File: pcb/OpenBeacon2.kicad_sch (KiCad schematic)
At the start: 74 parts, among them J1 Bias V, J10 UART, J11 BNC, J16 SMA CLKIN, J2 PAI+, J3 PAI-, J4 Digital IO, J5 ADC Inputs, J6 SMA, J8 I2C Bus, J9 GND, Q1 2N7002, Q2 MMBT4403, Q3 2SK3074, Q4 2N7002, Q5 2N7002, U1 TLV61046A, U2 ASTX-H11-25.000MHZ-T, U3 SN74LVC1G17, U4 SI5351C-B-GMR, U5 MCP4725A1T-E/CH, U6 128x32 OLED, U8 24AA64T

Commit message: BT1: KH-BS1220-2-SMT footprint from LCSC C5365932; J6/J16: Si5351BCBreakout SMA-ENDLAUNCH footprint, BWSMA-KE-P001 C496550; project-local OB2 footprint lib
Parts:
- J16: footprint EtherkitKicadLibrary:SMA-ENDLAUNCH -> OB2:SMA-ENDLAUNCH
- J6: footprint EtherkitKicadLibrary:SMA-ENDLAUNCH -> OB2:SMA-ENDLAUNCH; LCSC (none) -> C496550; MPN (none) -> BWSMA-KE-P001; Manufacturer (none) -> BAT Wireless
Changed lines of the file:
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@@
 			)
 		)
-		(property "Footprint" "EtherkitKicadLibrary:SMA-ENDLAUNCH"
-			(at 172.72 185.42 0)
-			(effects
-				(font
-					(size 1.27 1.27)
-				)
-				(hide yes)
-			)
-		)
-		(property "Datasheet" ""
+		(property "Footprint" "OB2:SMA-ENDLAUNCH"
+			(at 172.72 185.42 0)
+			(effects
+				(font
+					(size 1.27 1.27)
+				)
+				(hide yes)
+			)
+		)
+		(property "Datasheet" ""
+			(at 172.72 185.42 0)
+			(effects
+				(font
+					(size 1.27 1.27)
+				)
+				(hide yes)
+			)
+		)
+		(property "LCSC" "C496550"
+			(at 172.72 185.42 0)
+			(effects
+				(font
+					(size 1.27 1.27)
+				)
+				(hide yes)
+			)
+		)
+		(property "Manufacturer" "BAT Wireless"
+			(at 172.72 185.42 0)
+			(effects
+				(font
+					(size 1.27 1.27)
+				)
+				(hide yes)
+			)
+		)
+		(property "MPN" "BWSMA-KE-P001"
 			(at 172.72 185.42 0)
 			(effects
@@
 			)
 		)
-		(property "Footprint" "EtherkitKicadLibrary:SMA-ENDLAUNCH"
+		(property "Footprint" "OB2:SMA-ENDLAUNCH"
 			(at 33.02 220.98 0)
 			(effects

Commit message: Restore hand-wired root sheet, add Si5351C wired, split root across two A4 sheets
Root (A4) is the c2d4355 drawing with continuous wires: boost, keying, PA,
bias DAC, filter bank, BNC out, plus the Si5351C (U4, C14/C50-C53, J6 CLK2,
J16 CLKIN with R43/C54/R44/R45, R46 INTR pull-up, R47 CAL_CLK) drawn wired.
I/O headers, OLED/buttons, I2C level shift and EEPROM move unchanged to the
new io_ui.kicad_sch (A4). Netlist node sets identical to c569d37.
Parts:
- removed C1, C10, C11, C14, C17, C18, C19, C20, C21, C22, C23, C24, C5, C6, C8: 100n, Capacitor_SMD:C_0805_2012Metric, symbol Device:C_Small
- removed C2: 4.7u, Capacitor_SMD:C_0805_2012Metric, symbol Device:C_Small
- removed C3: 10u, Capacitor_SMD:C_0805_2012Metric, symbol Device:C_Small
- removed C4: 10n, Capacitor_SMD:C_0805_2012Metric, symbol Device:C_Small
- removed C50, C51, C52, C53, C54: 100n, Capacitor_SMD:C_0603_1608Metric, symbol Device:C_Small
- removed C7, C9: 1u, Capacitor_SMD:C_0805_2012Metric, symbol Device:C_Small
- removed J10: UART, Connector_PinHeader_2.54mm:PinHeader_1x04_P2.54mm_Vertical, symbol Connector_Generic:Conn_01x04
- removed J4: Digital IO, Connector_PinHeader_2.54mm:PinHeader_1x04_P2.54mm_Vertical, symbol Connector_Generic:Conn_01x04
- removed J5: ADC Inputs, Connector_PinHeader_2.54mm:PinHeader_1x06_P2.54mm_Vertical, symbol Connector_Generic:Conn_01x06
- removed J8: I2C Bus, Connector_PinHeader_2.54mm:PinHeader_1x04_P2.54mm_Vertical, symbol Connector_Generic:Conn_01x04
- removed Q4, Q5: 2N7002, EtherkitKicadLibrary:SOT23-2N7002, symbol EtherkitKicadLibrary:MOS_N
- removed R1, R2, R3: 22k, Resistor_SMD:R_0805_2012Metric, symbol Device:R_Small_US
- removed R11, R12, R14, R15, R5: 3.3k, Resistor_SMD:R_0805_2012Metric, symbol Device:R_Small_US
- removed R43: 49.9, Resistor_SMD:R_0603_1608Metric, symbol Device:R_Small_US
- removed R44, R45, R46: 10k, Resistor_SMD:R_0603_1608Metric, symbol Device:R_Small_US
- removed R47: 33, Resistor_SMD:R_0603_1608Metric, symbol Device:R_Small_US
- removed R6: 10, Resistor_SMD:R_0805_2012Metric, symbol Device:R_Small_US
- removed R7: 56, Resistor_SMD:R_0805_2012Metric, symbol Device:R_Small_US
- removed R8: 1 1%, Resistor_SMD:R_0805_2012Metric, symbol Device:R_Small_US
- removed S1: Menu 1, EtherkitKicadLibrary:Omron_B3F-1052, symbol EtherkitKicadLibrary:PUSHBUTTON_TACTILE
- removed S2: Menu 2, EtherkitKicadLibrary:Omron_B3F-1052, symbol EtherkitKicadLibrary:PUSHBUTTON_TACTILE
- removed S3: Left, EtherkitKicadLibrary:Omron_B3F-1052, symbol EtherkitKicadLibrary:PUSHBUTTON_TACTILE
- removed S4: Down, EtherkitKicadLibrary:Omron_B3F-1052, symbol EtherkitKicadLibrary:PUSHBUTTON_TACTILE
- removed S5: Up, EtherkitKicadLibrary:Omron_B3F-1052, symbol EtherkitKicadLibrary:PUSHBUTTON_TACTILE
- removed S6: Back, EtherkitKicadLibrary:Omron_B3F-1052, symbol EtherkitKicadLibrary:PUSHBUTTON_TACTILE
- removed S7: Right, EtherkitKicadLibrary:Omron_B3F-1052, symbol EtherkitKicadLibrary:PUSHBUTTON_TACTILE
- removed U6: 128x32 OLED, EtherkitKicadLibrary:128x32OLED, symbol EtherkitKicadLibrary:128x32OLED
- removed U8: 24AA64T, Package_TO_SOT_SMD:SOT-23-5, symbol EtherkitKicadLibrary:24AA64T
- added C1, C10, C11, C14, C5, C6, C8: 100n, Capacitor_SMD:C_0805_2012Metric, symbol EtherkitKicadLibrary:C
- added C2: 4.7u, Capacitor_SMD:C_0805_2012Metric, symbol EtherkitKicadLibrary:C
- added C3: 10u, Capacitor_SMD:C_0805_2012Metric, symbol EtherkitKicadLibrary:C
- added C4: 10n, Capacitor_SMD:C_0805_2012Metric, symbol EtherkitKicadLibrary:C
- added C50, C51, C52, C53, C54: 100n, Capacitor_SMD:C_0603_1608Metric, symbol EtherkitKicadLibrary:C
- added C7, C9: 1u, Capacitor_SMD:C_0805_2012Metric, symbol EtherkitKicadLibrary:C
- added R1, R2, R3: 22k, Resistor_SMD:R_0805_2012Metric, symbol EtherkitKicadLibrary:R
- added R43: 49.9, Resistor_SMD:R_0603_1608Metric, symbol EtherkitKicadLibrary:R
- added R44, R45, R46: 10k, Resistor_SMD:R_0603_1608Metric, symbol EtherkitKicadLibrary:R
- added R47: 33, Resistor_SMD:R_0603_1608Metric, symbol EtherkitKicadLibrary:R
- added R5: 3.3k, Resistor_SMD:R_0805_2012Metric, symbol EtherkitKicadLibrary:R
- added R6: 10, Resistor_SMD:R_0805_2012Metric, symbol EtherkitKicadLibrary:R
- added R7: 56, Resistor_SMD:R_0805_2012Metric, symbol EtherkitKicadLibrary:R
- added R8: 1 1%, Resistor_SMD:R_0805_2012Metric, symbol EtherkitKicadLibrary:R
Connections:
- net +3.3V: now also C14.1, C50.1, C51.1, C52.1, C53.1, C6.1, R44.1, R46.1
- net +5V: now also C1.1, C10.1, C2.1
- net CAL_CLK: now also R47.2
- net GND: now also C1.2, C10.2, C14.2, C2.2, C3.2, C50.2, C51.2, C52.2, C53.2, C6.2, C7.2, C9.2, R1.2, R43.2, R45.2
- net SI_INTR: now also R46.2
- net TX: now also R1.1
- net at J16.1 (In): now also C54.1, R43.1
- net at U4.19 (CLK4): now also R47.1
- net BOOST_SW: no longer names the net of L1.1, U1.1 (SW)
- net CLK2_SMA: no longer names the net of J6.1 (In), U4.9 (CLK2)
- net LPF_OUT renamed Filter Bank/LPF_OUT
- net PAI_N: no longer names the net of J3.1 (P1), L2.1
- net PAI_N: now also R8.1
- net PAI_P: no longer names the net of J2.1 (P1)
- net PAI_P: now also C7.1, R6.1, R8.2
- net PA_BIAS: no longer names the net of J1.1 (P1), U5.1 (VOUT)
- net PA_BIAS: now also C9.1, R7.2
- net PA_DRAIN: no longer names the net of L2.2, Q3.3 (D)
- net PA_DRAIN: now also C11.2, C8.1
- net PA_DRIVE: no longer names the net of U3.4
- net PA_DRIVE: now also C5.2, R5.2
- net PA_GATE: no longer names the net of Q3.2 (G)
- net PA_GATE: now also C5.1, R7.1
- net PA_SW_B: no longer names the net of Q2.2 (B)
- net PA_SW_B: now also C4.2, R2.2, R3.1
- net PA_VDD: no longer names the net of Q2.3 (C)
- net PA_VDD: now also C4.1, R6.2
- net SI_CLKIN: no longer names the net of U4.6 (CLKIN)
- net SI_CLKIN: now also C54.2, R44.2, R45.1
- net SI_XA: no longer names the net of R4.2, U4.1 (XA)
- net TCXO_OUT: no longer names the net of R4.1, U2.3 (OUT)
- net TX_N: no longer names the net of Q1.3 (D)
- net TX_N: now also R3.2
- net VBOOST: no longer names the net of Q2.1 (E), U1.5 (VO)
- net VBOOST: now also C3.1, R2.1
- new net: C8.2, R5.1
- new net Filter Bank/LPF_IN: C11.1
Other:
- added sheet I/O + UI (io_ui.kicad_sch)
- note added: "Boost Converter"
- note added: "Keying"
- note added: "Low-Pass Filter Bank (sheet 3)"
- note added: "PA Bias"
- note added: "Power Amplifier"
- note added: "Si5351C PLL"
- note removed: "12 V boost (TLV61046A)"
- note removed: "I/O headers"
- note removed: "I2C 3.3 V <-> 5 V level shift (OLED, DAC) + 24AA64 EEPROM"
- note removed: "J16 CLKIN (Si5351-B DS rev 1.3 Table 6, Table 16): 10-100 MHz, VIL < 0.3 VDD, VIH > 0.7 VDD, max 3.6 V; input not pulled internally. R43 terminates 50 ohm; C54 AC-couples; R44/R45 bias CLKIN at VDD/2. Sine needs >= 1.32 Vpp (+6.4 dBm) and <= 3.9 Vpp (+15.8 dBm). XB open (TCXO on XA, DS 6.6). OEB tied low = outputs enabled. INTR open drain, R46 10k (> 4.7k, DS Table 16) -> SI_INTR (PB3). CLK0 -> U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"
- note removed: "PAI+/PAI- = PA current-sense test points across R8 (1 ohm)."
- note removed: "Power amplifier (2SK3074) + bias DAC (MCP4725)"
- note removed: "Sub-sheets: Filter Bank (LPF_IN/LPF_OUT, BAND_A/B), MCU + USB (AVR128DA48, CP2102N, 3.3 V), GPS (MAX-M10S). They connect through the global labels."
- note removed: "Synth: Si5351C + 25 MHz TCXO on XA + external reference on CLKIN (J16)"
- note removed: "TX keying + PA supply switch"
- note removed: "U1 FB tied to VIN = fixed 12 V output (TLV61046A DS). C2 input, C3 output, both beside U1."
- note removed: "User interface: OLED + buttons (100n debounce beside each button)"

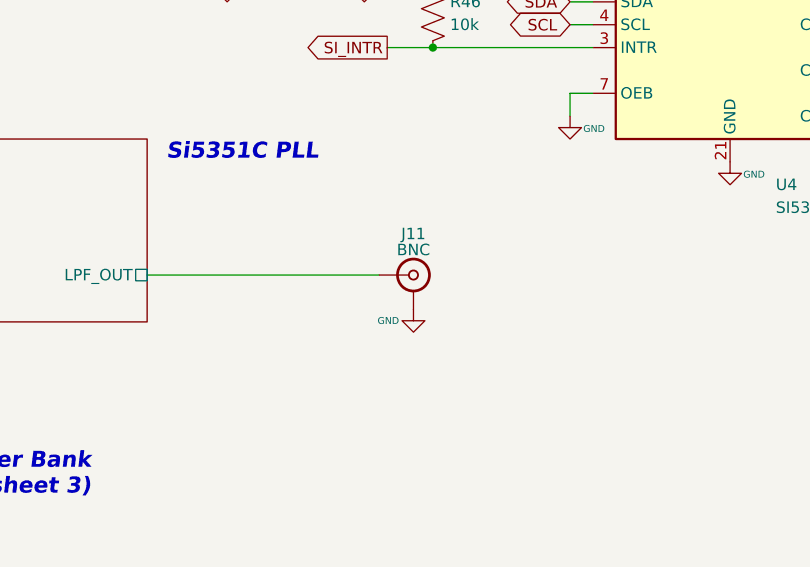
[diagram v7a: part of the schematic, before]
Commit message: J11: Amphenol RF 031-5431-10RFX MPN; mark DNP and exclude from position files (hand-soldered)
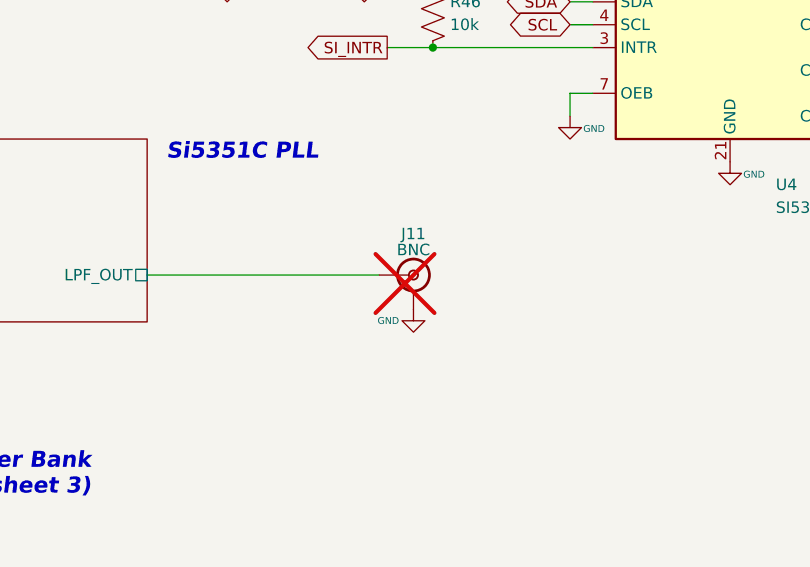
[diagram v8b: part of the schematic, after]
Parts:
- J11: MPN (none) -> 031-5431-10RFX; Manufacturer (none) -> Amphenol RF; now not fitted
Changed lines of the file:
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@@
 		(in_bom yes)
 		(on_board yes)
-		(in_pos_files yes)
-		(dnp no)
+		(in_pos_files no)
+		(dnp yes)
 		(property "Reference" "J11"
 			(at 195.961 109.601 0)
@@
 			)
 		)
+		(property "MPN" "031-5431-10RFX"
+			(at 195.961 114.173 0)
+			(effects
+				(font
+					(size 1.27 1.27)
+				)
+				(hide yes)
+			)
+		)
+		(property "Manufacturer" "Amphenol RF"
+			(at 195.961 114.173 0)
+			(effects
+				(font
+					(size 1.27 1.27)
+				)
+				(hide yes)
+			)
+		)
